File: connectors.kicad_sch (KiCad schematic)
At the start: 11 parts, among them J10 SM02B-SRSS-TB(LF)(SN), J11 SM02B-SRSS-TB(LF)(SN), J6 SM04B-SRSS-TB(LF)(SN), J7 SM04B-SRSS-TB(LF)(SN), J8 SM04B-SRSS-TB(LF)(SN), J9 SM04B-SRSS-TB(LF)(SN)

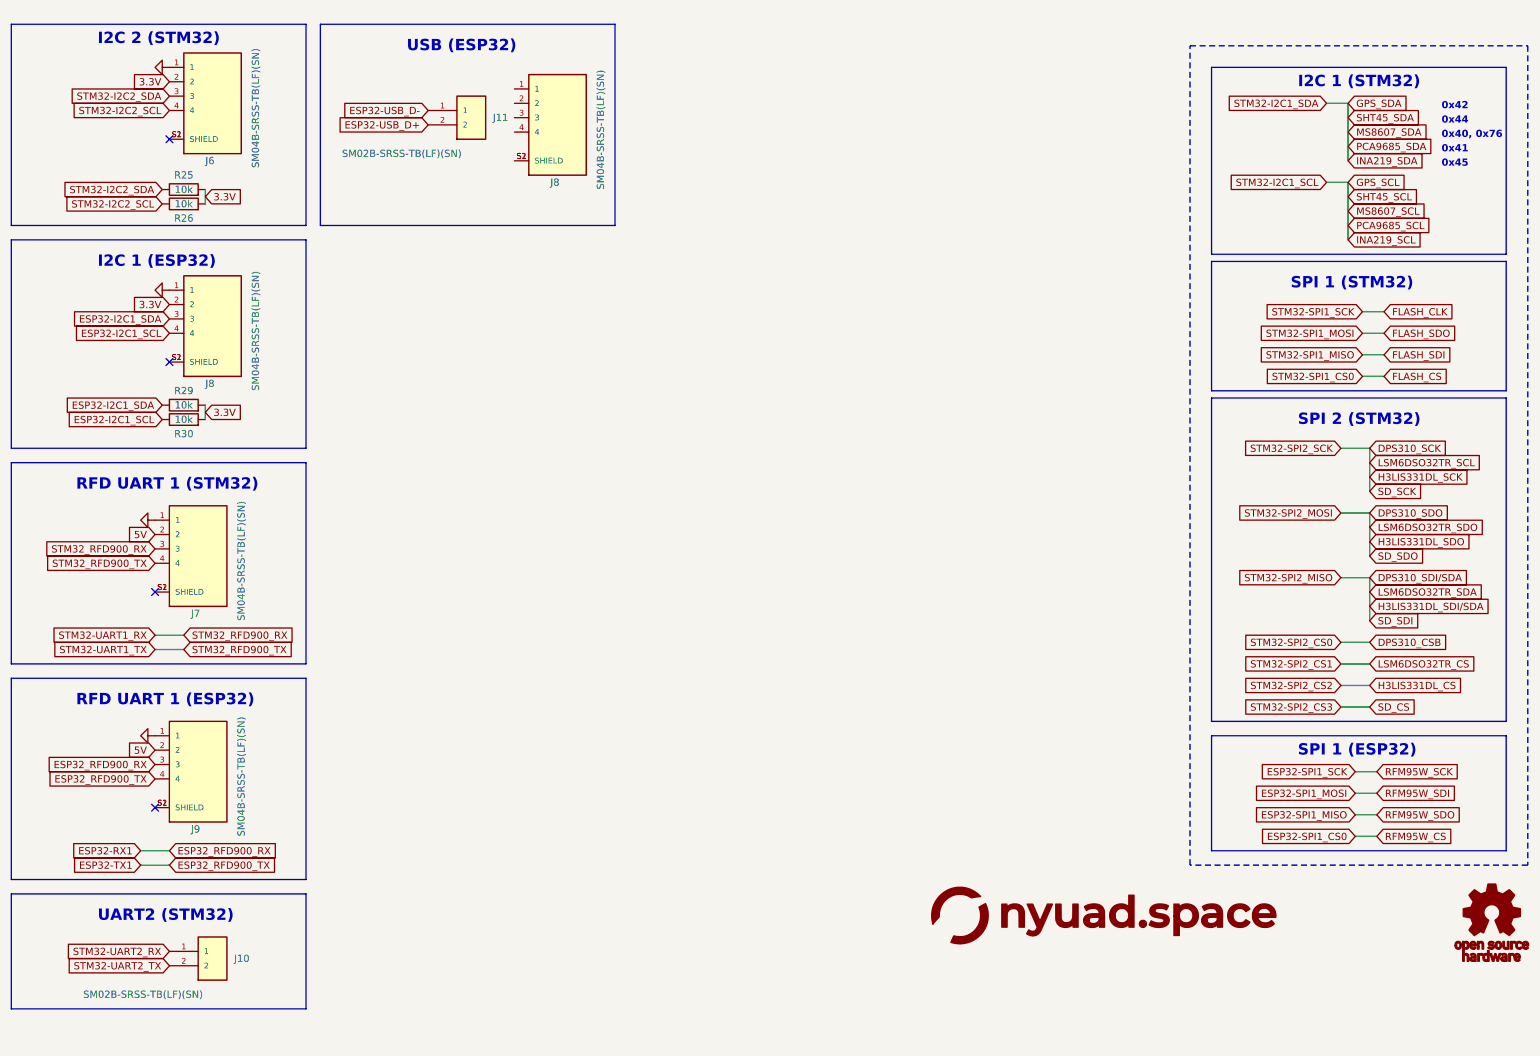
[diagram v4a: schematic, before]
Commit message: Added connectors
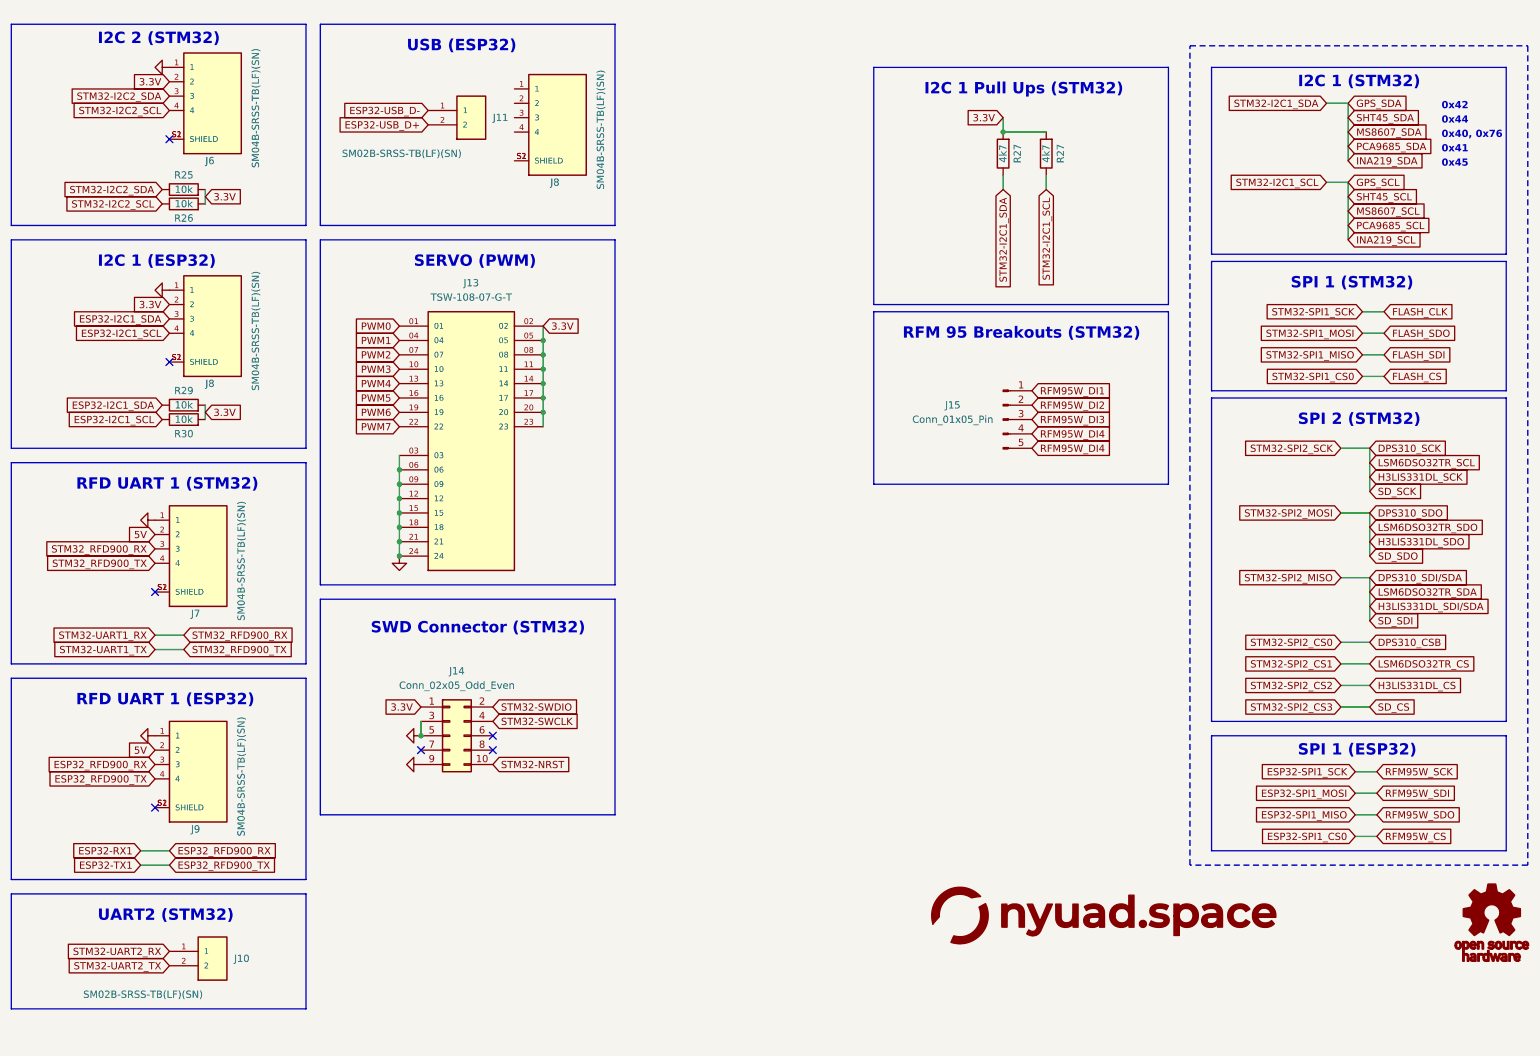
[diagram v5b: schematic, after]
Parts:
- added J13: TSW-108-07-G-T, TSW-108-07-G-T:SAMTEC_TSW-108-07-G-T, symbol TSW-108-07-G-T:TSW-108-07-G-T
- added J14: Conn_02x05_Odd_Even, symbol Connector_Generic:Conn_02x05_Odd_Even
- added J15: Conn_01x05_Pin, symbol Connector:Conn_01x05_Pin
- added R27 (x2): 4k7, Resistor_SMD:R_0201_0603Metric, symbol Device:R
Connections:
- net 3.3V: now also J13.02, J13.05, J13.08, J13.11, J13.14, J13.17, J13.20, J13.23, J14.1 (Pin_1), R27.2, R27.2
- net GND: now also J13.03, J13.06, J13.09, J13.12, J13.15, J13.18, J13.21, J13.24, J14.3 (Pin_3), J14.5 (Pin_5), J14.9 (Pin_9)
- net GPS_SCL: now also R27.1
- net GPS_SDA: now also R27.1
- new net PWM0: J13.01
- new net PWM1: J13.04
- new net PWM2: J13.07
- new net PWM3: J13.10
- new net PWM4: J13.13
- new net PWM5: J13.16
- new net PWM6: J13.19
- new net PWM7: J13.22
- new net RFM95W_DI1: J15.1 (Pin_1)
- new net RFM95W_DI2: J15.2 (Pin_2)
- new net RFM95W_DI3: J15.3 (Pin_3)
- new net RFM95W_DI4: J15.4 (Pin_4), J15.5 (Pin_5)
- new net STM32-NRST: J14.10 (Pin_10)
- new net STM32-SWCLK: J14.4 (Pin_4)
- new net STM32-SWDIO: J14.2 (Pin_2)
- no-connect marks 4 -> 7
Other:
- note added: "I2C 1 Pull Ups (STM32)"
- note added: "RFM 95 Breakouts (STM32)"
- note added: "SERVO (PWM)"
- note added: "SWD Connector (STM32)"

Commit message: updated footprint library
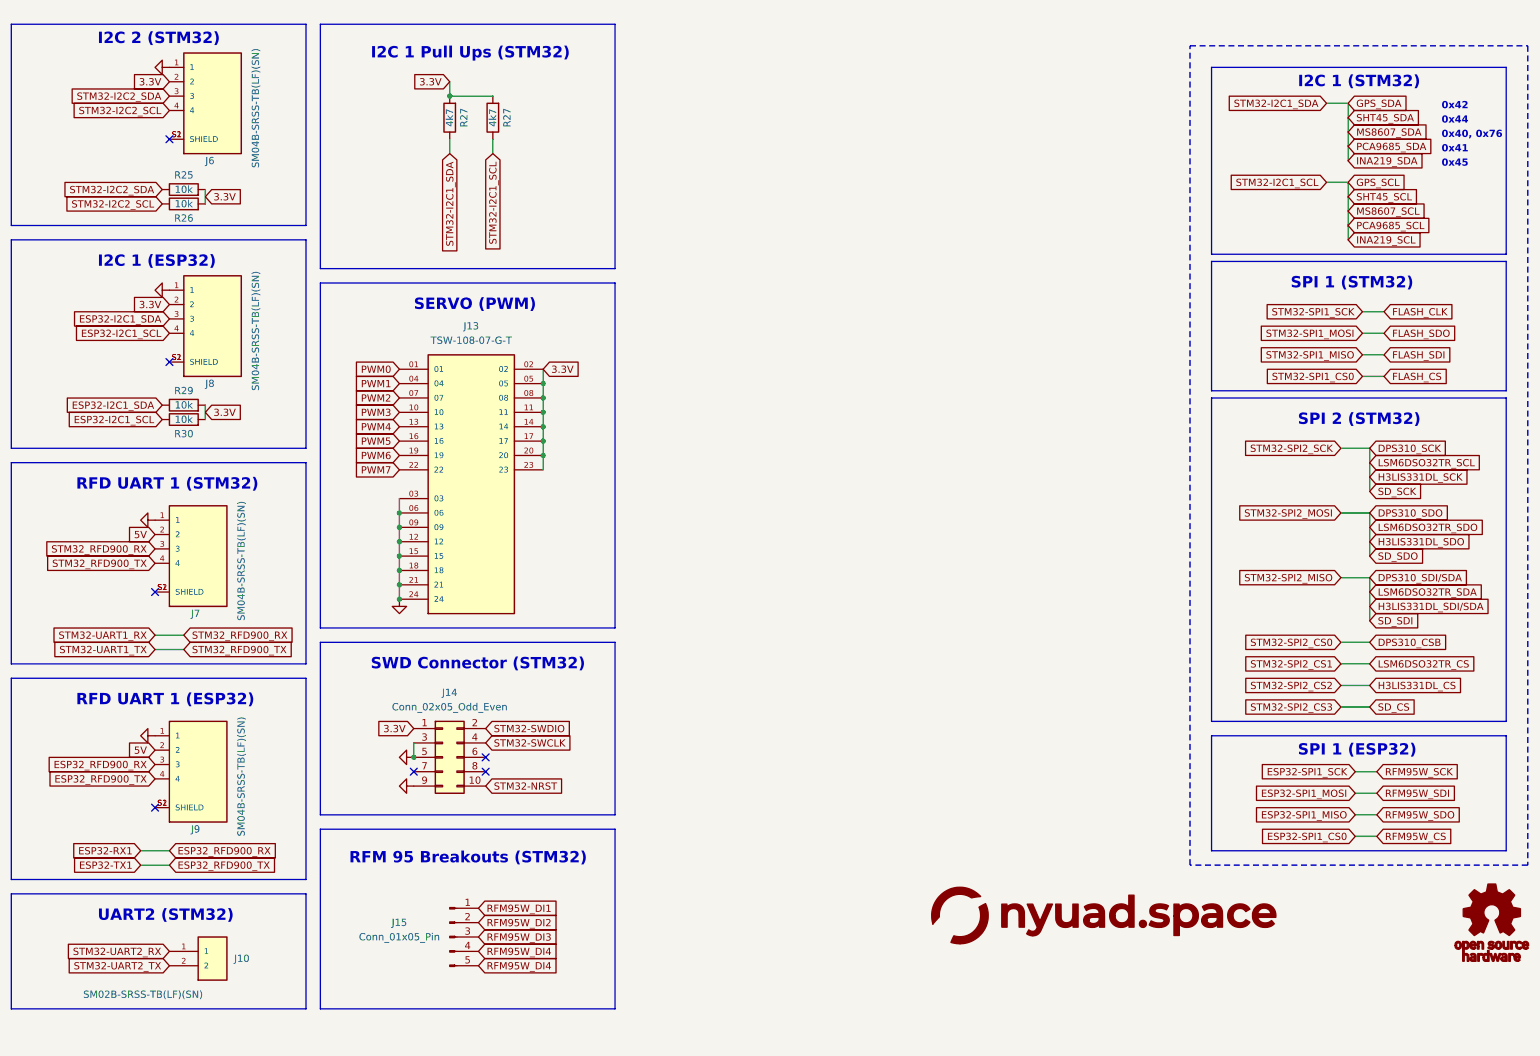
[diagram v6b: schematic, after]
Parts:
- removed J11: SM02B-SRSS-TB(LF)(SN), SM02B-SRSS-TB(LF)(SN), symbol SM02B-SRSS-TB_LF__SN_:SM02B-SRSS-TB(LF)(SN)
- removed J8: SM04B-SRSS-TB(LF)(SN), JST_SM04B-SRSS-TB(LF)(SN), symbol SM04B-SRSS-TB_LF__SN_:SM04B-SRSS-TB(LF)(SN)
- R25, R26, R29, R30: footprint Resistor_SMD:R_0201_0603Metric -> Resistor_SMD:R_0402_1005Metric
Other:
- note removed: "USB (ESP32)"
- moved on the sheet: J13, J14, J15, R27

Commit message: Updated symbol footprints
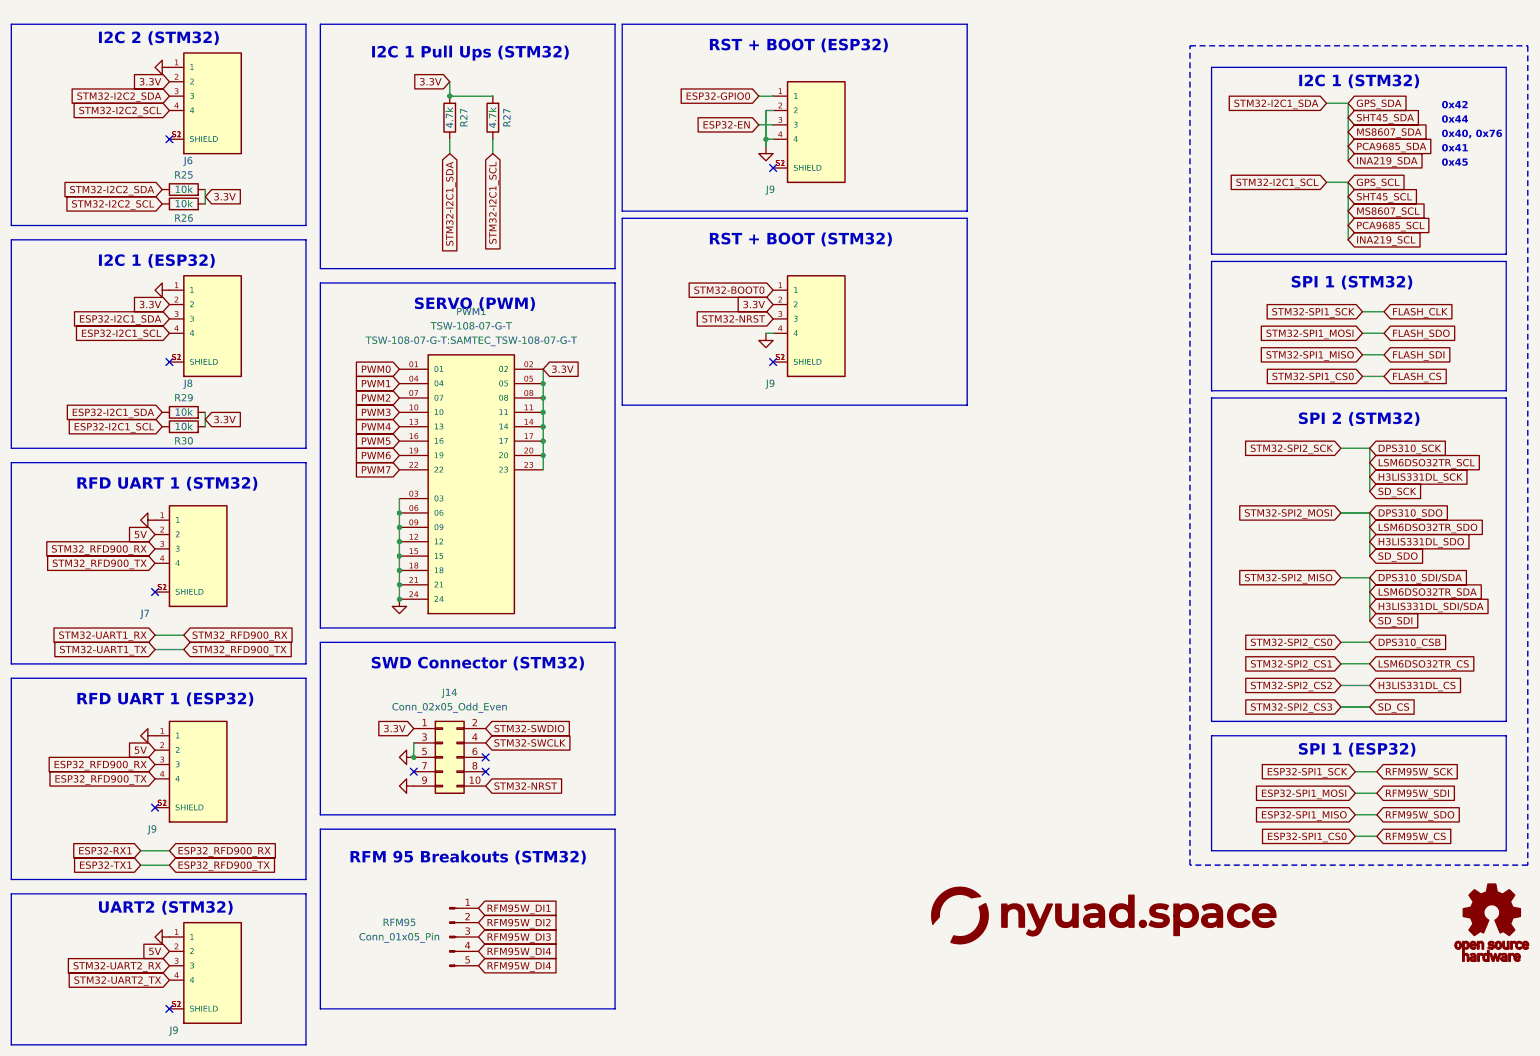
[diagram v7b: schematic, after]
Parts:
- removed J10: SM02B-SRSS-TB(LF)(SN), SM02B-SRSS-TB(LF)(SN), symbol SM02B-SRSS-TB_LF__SN_:SM02B-SRSS-TB(LF)(SN)
- added J9 (x3): SM04B-SRSS-TB(LF)(SN), JST_SM04B-SRSS-TB(LF)(SN), symbol SM04B-SRSS-TB_LF__SN_:SM04B-SRSS-TB(LF)(SN)
- J14: footprint (none) -> Connector_PinHeader_1.27mm:PinHeader_2x05_P1.27mm_Vertical_SMD
- R25, R26, R29, R30: footprint Resistor_SMD:R_0402_1005Metric -> Resistor_SMD:R_0603_1608Metric
- R27: value 4k7 -> 4.7k; footprint Resistor_SMD:R_0201_0603Metric -> Resistor_SMD:R_0402_1005Metric
- RFM95: renamed from J15; footprint (none) -> Connector_PinHeader_1.27mm:PinHeader_1x05_P1.27mm_Vertical
- renumbered J13 to PWM1
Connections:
- net 3.3V: now also J9.2
- net 5V: now also J9.2
- net GND: now also J9.1, J9.2, J9.4, J9.4
- net STM32-NRST: now also J9.3
- net STM32-UART2_RX: now also J9.3
- net STM32-UART2_TX: now also J9.4
- new net: J9.S1 (SHIELD), J9.S2 (SHIELD) (x3)
- new net ESP32-EN: J9.3
- new net ESP32-GPIO0: J9.1
- new net STM32-BOOT0: J9.1
- no-connect marks 7 -> 10
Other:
- note added: "RST + BOOT (ESP32)"
- note added: "RST + BOOT (STM32)"
- moved on the sheet: R29, R30

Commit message: updated schematic
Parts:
- renumbered J7 to J?, J9 to J?, J14 to J?, J8 to J?, J6 to J?, R27 to R?, R25 to R?, R29 to R?, R26 to R?, R30 to R?, RFM95 to RFM2
